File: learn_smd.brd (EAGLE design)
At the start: 35.6 x 40.6 mm, 11 parts, among them Q1 MMBT2222A, Q2 MMBT2222A

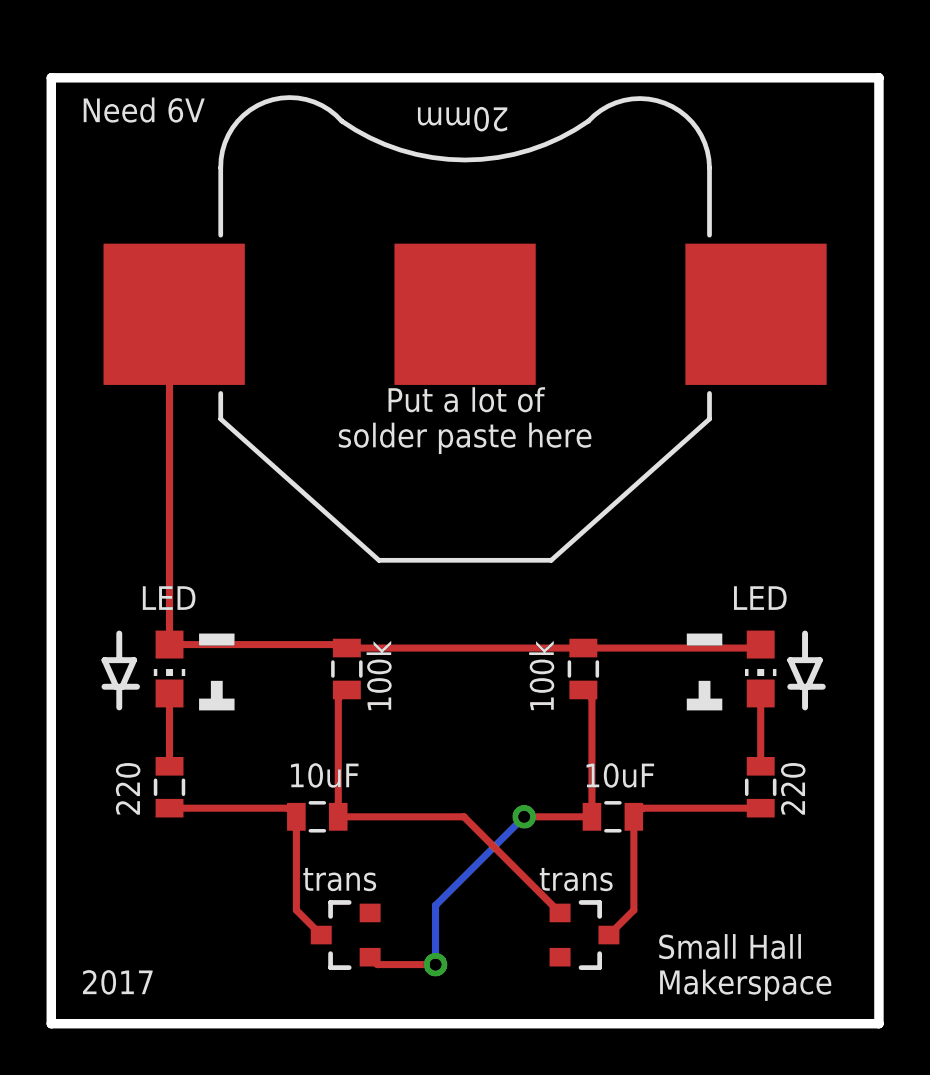
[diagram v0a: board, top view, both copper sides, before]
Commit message: switched to through hole battery
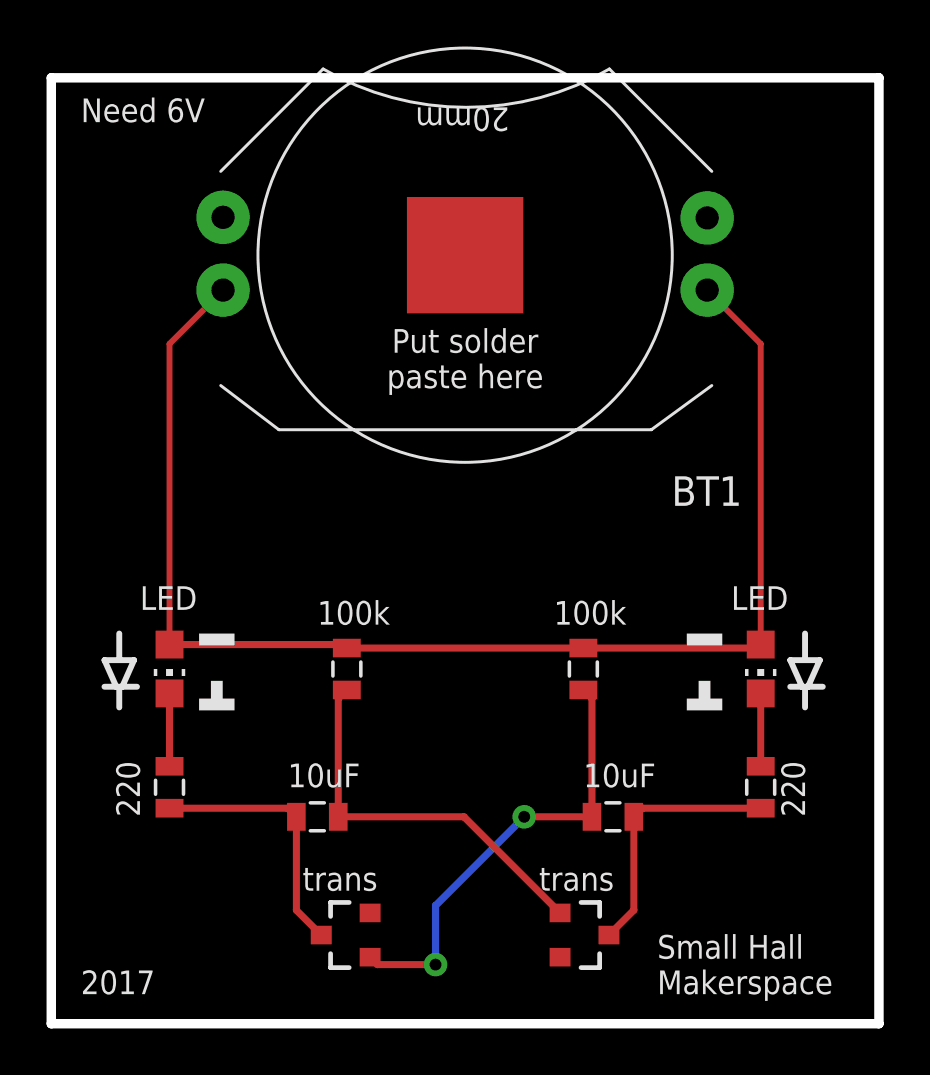
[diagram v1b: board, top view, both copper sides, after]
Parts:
- removed BAT1: (no value), SparkFun-Electromechanical:BATTCON_20MM
- added BT1: BAT-HLD-001-THM, BAT-HLD-001-THM:LINX_BAT-HLD-001-THM
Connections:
- net GND: now also BT1.-; no longer BAT1.2
- net N$6: now also BT1.+@1, BT1.+@2, BT1.+@3, BT1.+@4; no longer BAT1.1
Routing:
- net N$6: track 42.4 -> 58.0 mm
- added copper zone on layer 16, net N$8
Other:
- board text added: "Put solder paste here"
- board text removed: "Put a lot of solder paste here"
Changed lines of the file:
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@@
 <setting verticaltext="up"/>
 </settings>
-<grid distance="0.025" unitdist="inch" unit="inch" style="lines" multiple="1" display="yes" altdistance="0.005" altunitdist="inch" altunit="inch"/>
+<grid distance="0.05" unitdist="inch" unit="inch" style="lines" multiple="1" display="yes" altdistance="0.005" altunitdist="inch" altunit="inch"/>
 <layers>
 <layer number="1" name="Top" color="4" fill="1" visible="yes" active="yes"/>
@@
 <wire x1="35.56" y1="40.64" x2="0" y2="40.64" width="0.4064" layer="20"/>
 <wire x1="0" y1="40.64" x2="0" y2="0" width="0.4064" layer="20"/>
-<text x="14.605" y="13.335" size="1.016" layer="21" font="vector" ratio="15" rot="R90">100k</text>
-<text x="21.59" y="13.335" size="1.016" layer="21" font="vector" ratio="15" rot="R90">100k</text>
+<text x="11.43" y="17.145" size="1.016" layer="21" font="vector" ratio="15">100k</text>
+<text x="21.59" y="17.145" size="1.016" layer="21" font="vector" ratio="15">100k</text>
 <text x="10.16" y="10.16" size="1.016" layer="21" font="vector" ratio="15">10uF</text>
 <text x="22.86" y="10.16" size="1.016" layer="21" font="vector" ratio="15">10uF</text>
@@
 <text x="3.81" y="17.78" size="1.016" layer="21" font="vector" ratio="15">LED</text>
 <text x="29.21" y="17.78" size="1.016" layer="21" font="vector" ratio="15">LED</text>
-<text x="17.78" y="26.035" size="1.016" layer="21" font="vector" ratio="15" align="center">Put a lot of
-solder paste here</text>
+<text x="17.78" y="28.575" size="1.016" layer="21" font="vector" ratio="15" align="center">Put solder
+paste here</text>
 <text x="10.795" y="5.715" size="1.016" layer="21" ratio="15">trans</text>
 <text x="20.955" y="5.715" size="1.016" layer="21" ratio="15">trans</text>
@@
 </autorouter>
 <elements>
-<element name="BAT1" library="SparkFun-Electromechanical" package="BATTCON_20MM" value="" x="17.78" y="30.48" smashed="yes">
-<attribute name="VALUE" x="10.795" y="29.845" size="0.4064" layer="27"/>
-</element>
 <element name="C1" library="SparkFun-Capacitors" package="0805" value="10uF" x="24.13" y="8.89" smashed="yes" rot="R180"/>
 <element name="C2" library="SparkFun-Capacitors" package="0805" value="10uF" x="11.43" y="8.89" smashed="yes" rot="R180"/>
@@
 <element name="R3" library="SparkFun-Passives" package="0805" value="100k" x="12.7" y="15.24" smashed="yes" rot="R270"/>
 <element name="R4" library="SparkFun-Passives" package="0805" value="100k" x="22.86" y="15.24" smashed="yes" rot="R270"/>
+<element name="BT1" library="BAT-HLD-001-THM" package="LINX_BAT-HLD-001-THM" value="BAT-HLD-001-THM" x="17.78" y="33.02" rot="R180">
+<attribute name="COST1000" value="0.196" x="17.78" y="33.02" size="1.778" layer="27" font="vector" ratio="15" rot="R180" display="off"/>
+<attribute name="LINK_B" value="http://www.mouser.com/ProductDetail/Panasonic-Battery/CR2016/" x="17.78" y="33.02" size="1.778" layer="27" font="vector" ratio="15" rot="R180" display="off"/>
+<attribute name="LINK" value="http://www.mouser.com/ProductDetail/Linx-Technologies/BAT-HLD-001-THM/" x="17.78" y="33.02" size="1.778" layer="27" font="vector" ratio="15" rot="R180" display="off"/>
+<attribute name="COST1000_B" value="0.184" x="17.78" y="33.02" size="1.778" layer="27" font="vector" ratio="15" rot="R180" display="off"/>
+</element>
 </elements>
 <signals>
@@
 <contactref element="R3" pad="1"/>
 <contactref element="R4" pad="1"/>
-<contactref element="BAT1" pad="1"/>
-<wire x1="5.28" y1="30.48" x2="5.08" y2="31.75" width="0.3048" layer="1"/>
-<wire x1="5.08" y1="31.75" x2="5.08" y2="16.29" width="0.3048" layer="1"/>
 <wire x1="30.48" y1="16.14" x2="30.48" y2="16.29" width="0.3048" layer="1"/>
 <wire x1="5.08" y1="16.29" x2="12.55" y2="16.29" width="0.3048" layer="1"/>
@@
 <wire x1="22.86" y1="16.14" x2="30.33" y2="16.14" width="0.3048" layer="1"/>
 <wire x1="30.33" y1="16.14" x2="30.48" y2="16.29" width="0.3048" layer="1"/>
+<contactref element="BT1" pad="+@3"/>
+<contactref element="BT1" pad="+@1"/>
+<contactref element="BT1" pad="+@2"/>
+<contactref element="BT1" pad="+@4"/>
+<wire x1="7.38" y1="31.52" x2="7.38" y2="31.51" width="0.254" layer="1"/>
+<wire x1="7.38" y1="31.51" x2="5.08" y2="29.21" width="0.254" layer="1"/>
+<wire x1="5.08" y1="29.21" x2="5.08" y2="16.29" width="0.254" layer="1"/>
+<wire x1="28.18" y1="31.52" x2="28.18" y2="31.51" width="0.254" layer="1"/>
+<wire x1="28.18" y1="31.51" x2="30.48" y2="29.21" width="0.254" layer="1"/>
+<wire x1="30.48" y1="29.21" x2="30.48" y2="16.29" width="0.254" layer="1"/>
+<wire x1="28.18" y1="31.52" x2="28.18" y2="34.62" width="0" layer="19" extent="1-1"/>
+<wire x1="7.38" y1="34.647" x2="7.38" y2="31.52" width="0" layer="19" extent="1-1"/>
 </signal>
 <signal name="N$7">
@@
 <contactref element="Q1" pad="2"/>
 <contactref element="Q2" pad="2"/>
-<contactref element="BAT1" pad="2"/>
 <polygon width="0.3048" layer="1" isolate="0.3048">
 <vertex x="0" y="0"/>
@@
 <vertex x="35.56" y="0"/>
 </polygon>
-</signal>
+<contactref element="BT1" pad="-"/>
+</signal>
+<signal name="N$8">
+<polygon width="0.254" layer="16" isolate="0.3048">
+<vertex x="0" y="40.64"/>
+<vertex x="35.56" y="40.64"/>
+<vertex x="35.56" y="0"/>
+<vertex x="0" y="0"/>
+</polygon>
+</signal>

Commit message: resized board
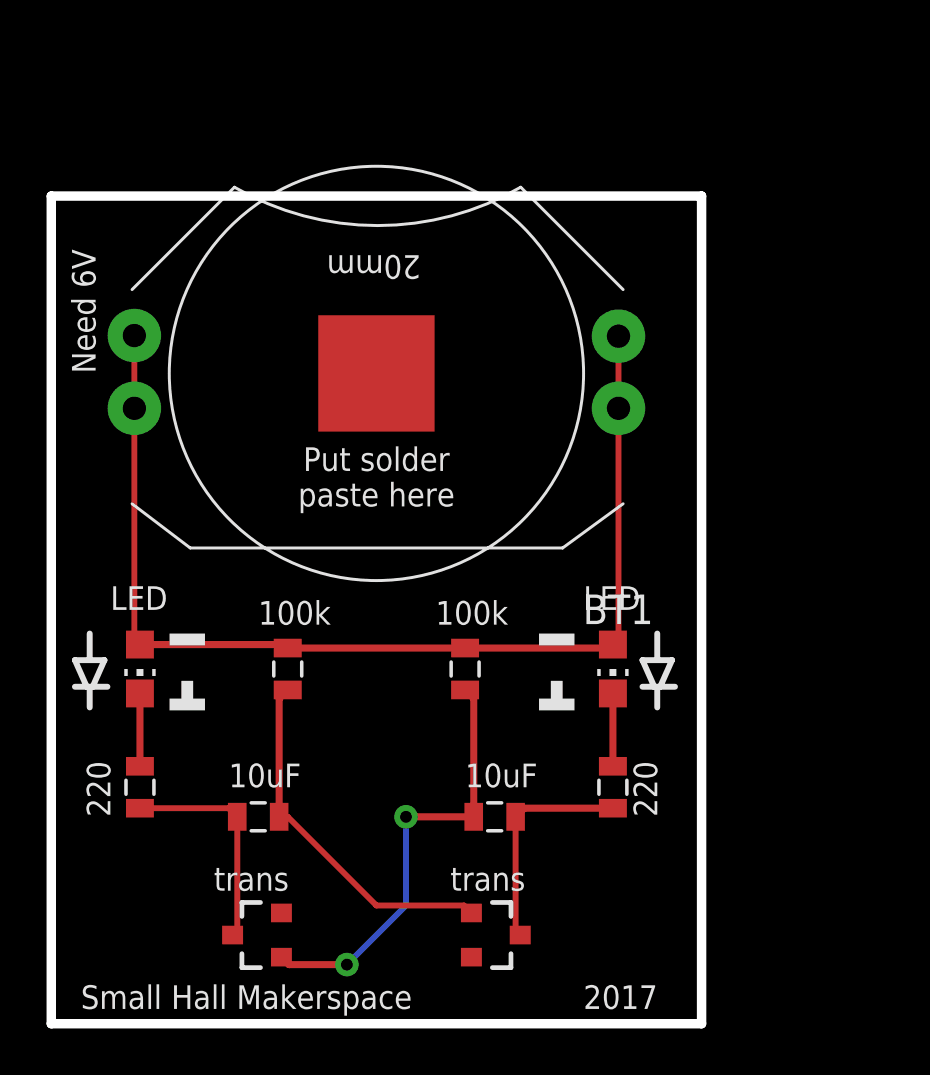
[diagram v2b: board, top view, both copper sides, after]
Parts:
- moved BT1 6.35 mm to (14.0, 27.9)
- moved LED2 6.35 mm to (24.1, 15.2)
- moved R2 6.35 mm to (24.1, 10.2)
- moved C1 5.08 mm to (19.1, 8.89)
- moved R4 5.08 mm to (17.8, 15.2)
- moved Q1 3.81 mm to (8.89, 3.81)
- moved Q2 3.81 mm to (19.1, 3.81)
- moved C2 2.54 mm to (8.89, 8.89)
- moved R3 2.54 mm to (10.2, 15.2)
- moved LED1 1.27 mm to (3.81, 15.2)
- moved R1 1.27 mm to (3.81, 10.2)
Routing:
- net N$6: track 58.0 -> 47.3 mm
- net N$4: track 11.1 -> 9.50 mm
- net N$2: track 11.1 -> 9.50 mm
- net N$7: track 16.8 -> 15.6 mm
- net N$3: track 19.4 -> 18.9 mm
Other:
- board size 35.6 x 40.6 mm -> 27.9 x 35.6 mm

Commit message: increase battery overhang
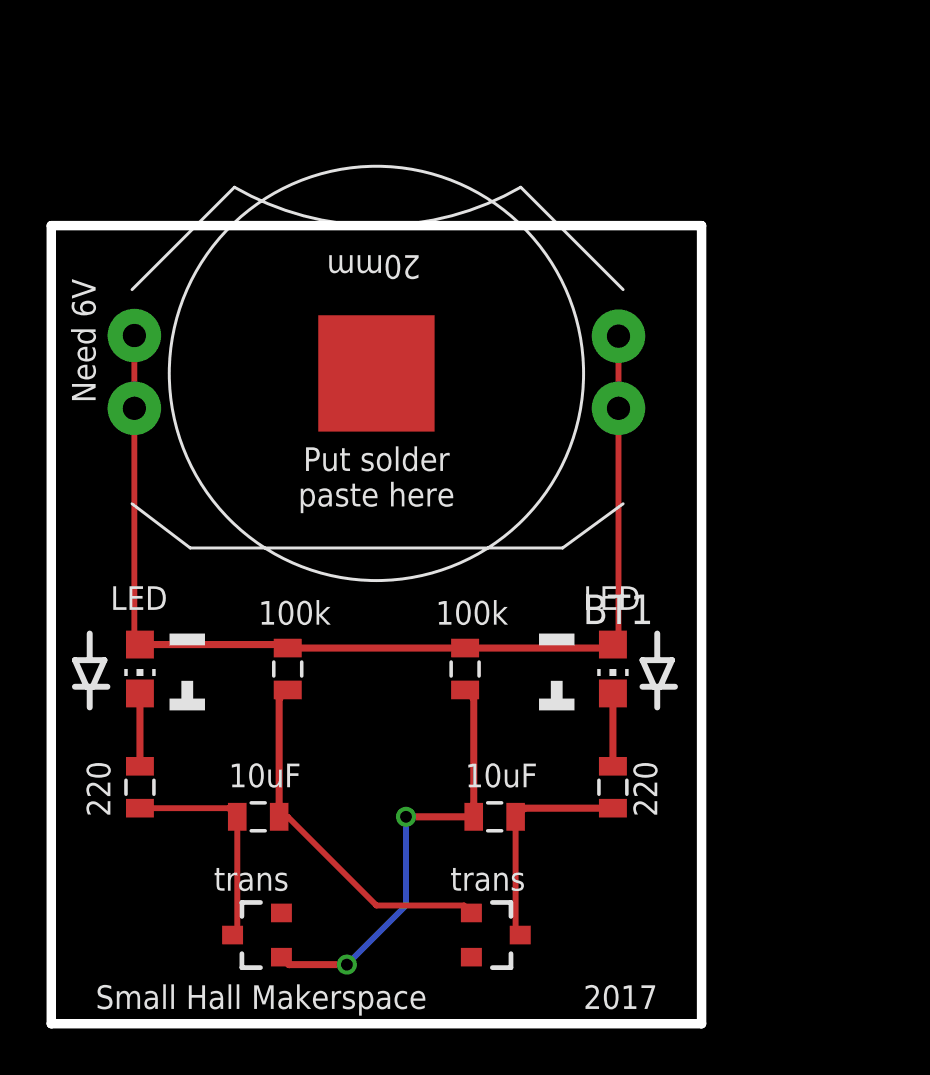
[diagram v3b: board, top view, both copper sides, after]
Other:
- board size 27.9 x 35.6 mm -> 27.9 x 34.3 mm
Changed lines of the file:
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@@
 <plain>
 <wire x1="0" y1="0" x2="27.94" y2="0" width="0.4064" layer="20"/>
-<wire x1="27.94" y1="0" x2="27.94" y2="35.56" width="0.4064" layer="20"/>
-<wire x1="27.94" y1="35.56" x2="0" y2="35.56" width="0.4064" layer="20"/>
-<wire x1="0" y1="35.56" x2="0" y2="0" width="0.4064" layer="20"/>
+<wire x1="27.94" y1="0" x2="27.94" y2="34.29" width="0.4064" layer="20"/>
+<wire x1="27.94" y1="34.29" x2="0" y2="34.29" width="0.4064" layer="20"/>
+<wire x1="0" y1="34.29" x2="0" y2="0" width="0.4064" layer="20"/>
 <text x="8.89" y="17.145" size="1.016" layer="21" font="vector" ratio="15">100k</text>
 <text x="16.51" y="17.145" size="1.016" layer="21" font="vector" ratio="15">100k</text>
@@
 <text x="15.875" y="33.02" size="1.016" layer="21" ratio="15" rot="SR180">20mm</text>
 <text x="22.86" y="0.635" size="1.016" layer="21" ratio="15">2017</text>
-<text x="1.27" y="0.635" size="1.016" layer="21" ratio="15">Small Hall Makerspace</text>
+<text x="1.905" y="0.635" size="1.016" layer="21" ratio="15">Small Hall Makerspace</text>
 <text x="13.97" y="29.21" size="1.016" layer="22" ratio="15" rot="MR0" align="center">Surface Mount Solder
 Practice Board</text>
@@
 3) Put in Reflow Oven</text>
 <text x="13.97" y="4.445" size="1.016" layer="22" ratio="15" rot="MR0" align="center">Designed by William Laney</text>
-<text x="1.905" y="27.94" size="1.016" layer="21" font="vector" ratio="15" rot="R90">Need 6V</text>
+<text x="1.905" y="26.67" size="1.016" layer="21" font="vector" ratio="15" rot="R90">Need 6V</text>
 </plain>
 <attributes>
@@
 </class>
 </classes>
-<designrules name="SparkFun">
-<description language="en">&lt;b&gt;EAGLE Design Rules&lt;/b&gt;
+<designrules name="oshpark-2layer">
+<description language="de">&lt;b&gt;EAGLE Design Rules&lt;/b&gt;
 &lt;p&gt;
-The default Design Rules have been set to cover
-a wide range of applications. Your particular design
-may have different requirements, so please make the
-necessary adjustments and save your customized
-design rules under a new name.</description>
+Die Standard-Design-Rules sind so gewählt, dass sie für
+die meisten Anwendungen passen. Sollte ihre Platine
+besondere Anforderungen haben, treffen Sie die erforderlichen
+Einstellungen hier und speichern die Design Rules unter
+einem neuen Namen ab.</description>
+<description language="en">&lt;b&gt;Laen's PCB Order Design Rules&lt;/b&gt;
+&lt;p&gt;
+Please make sure your boards conform to these design rules.</description>
 <param name="layerSetup" value="(1*16)"/>
-<param name="mtCopper" value="0.035mm 0.035mm 0.035mm 0.035mm 0.035mm 0.035mm 0.035mm 0.035mm 0.035mm 0.035mm 0.035mm 0.035mm 0.035mm 0.035mm 0.035mm 0.035mm"/>
-<param name="mtIsolate" value="1.5mm 0.15mm 0.2mm 0.15mm 0.2mm 0.15mm 0.2mm 0.15mm 0.2mm 0.15mm 0.2mm 0.15mm 0.2mm 0.15mm 0.2mm"/>
-<param name="mdWireWire" value="8mil"/>
-<param name="mdWirePad" value="8mil"/>
-<param name="mdWireVia" value="8mil"/>
-<param name="mdPadPad" value="8mil"/>
-<param name="mdPadVia" value="8mil"/>
-<param name="mdViaVia" value="8mil"/>
-<param name="mdSmdPad" value="8mil"/>
-<param name="mdSmdVia" value="8mil"/>
-<param name="mdSmdSmd" value="8mil"/>
+<param name="mtCopper" value="0.0356mm 0.0356mm 0.0356mm 0.0356mm 0.0356mm 0.0356mm 0.0356mm 0.0356mm 0.0356mm 0.0356mm 0.0356mm 0.0356mm 0.0356mm 0.0356mm 0.0356mm 0.0356mm"/>
+<param name="mtIsolate" value="1.5011mm 0.1499mm 0.2007mm 0.1499mm 0.2007mm 0.1499mm 0.2007mm 0.1499mm 0.2007mm 0.1499mm 0.2007mm 0.1499mm 0.2007mm 0.1499mm 0.2007mm"/>
+<param name="mdWireWire" value="6mil"/>
+<param name="mdWirePad" value="6mil"/>
+<param name="mdWireVia" value="6mil"/>
+<param name="mdPadPad" value="6mil"/>
+<param name="mdPadVia" value="6mil"/>
+<param name="mdViaVia" value="6mil"/>
+<param name="mdSmdPad" value="6mil"/>
+<param name="mdSmdVia" value="6mil"/>
+<param name="mdSmdSmd" value="6mil"/>
 <param name="mdViaViaSameLayer" value="8mil"/>
 <param name="mnLayersViaInSmd" value="2"/>
-<param name="mdCopperDimension" value="8mil"/>
-<param name="mdDrill" value="8mil"/>
+<param name="mdCopperDimension" value="15mil"/>
+<param name="mdDrill" value="6mil"/>
 <param name="mdSmdStop" value="0mil"/>
-<param name="msWidth" value="8mil"/>
-<param name="msDrill" value="20mil"/>
-<param name="msMicroVia" value="9.99mm"/>
+<param name="msWidth" value="6mil"/>
+<param name="msDrill" value="13mil"/>
+<param name="msMicroVia" value="13mil"/>
 <param name="msBlindViaRatio" value="0.5"/>
 <param name="rvPadTop" value="0.25"/>
@@
 <param name="rvMicroViaOuter" value="0.25"/>
 <param name="rvMicroViaInner" value="0.25"/>
-<param name="rlMinPadTop" value="12mil"/>
+<param name="rlMinPadTop" value="7mil"/>
 <param name="rlMaxPadTop" value="20mil"/>
-<param name="rlMinPadInner" value="10mil"/>
+<param name="rlMinPadInner" value="7mil"/>
 <param name="rlMaxPadInner" value="20mil"/>
-<param name="rlMinPadBottom" value="12mil"/>
+<param name="rlMinPadBottom" value="7mil"/>
 <param name="rlMaxPadBottom" value="20mil"/>
-<param name="rlMinViaOuter" value="10mil"/>
+<param name="rlMinViaOuter" value="7mil"/>
 <param name="rlMaxViaOuter" value="20mil"/>
-<param name="rlMinViaInner" value="10mil"/>
+<param name="rlMinViaInner" value="7mil"/>
 <param name="rlMaxViaInner" value="20mil"/>
 <param name="rlMinMicroViaOuter" value="4mil"/>
@@
 <param name="mvStopFrame" value="1"/>
 <param name="mvCreamFrame" value="0"/>
-<param name="mlMinStopFrame" value="4mil"/>
-<param name="mlMaxStopFrame" value="4mil"/>
+<param name="mlMinStopFrame" value="2.5mil"/>
+<param name="mlMaxStopFrame" value="2.5mil"/>
 <param name="mlMinCreamFrame" value="0mil"/>
 <param name="mlMaxCreamFrame" value="0mil"/>
-<param name="mlViaStopLimit" value="20mil"/>
+<param name="mlViaStopLimit" value="0mil"/>
 <param name="srRoundness" value="0"/>
 <param name="srMinRoundness" value="0mil"/>
@@
 <polygon width="0.3048" layer="1" isolate="0.3048">
 <vertex x="0" y="0"/>
-<vertex x="0" y="35.56"/>
-<vertex x="27.94" y="35.56"/>
+<vertex x="0" y="34.29"/>
+<vertex x="27.94" y="34.29"/>
 <vertex x="27.94" y="0"/>
 </polygon>
@@
 <signal name="N$8">
 <polygon width="0.254" layer="16" isolate="0.3048">
-<vertex x="0" y="35.56"/>
-<vertex x="27.94" y="35.56"/>
+<vertex x="0" y="34.29"/>
+<vertex x="27.94" y="34.29"/>
 <vertex x="27.94" y="0"/>
 <vertex x="0" y="0"/>
